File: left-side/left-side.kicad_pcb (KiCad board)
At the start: 2 copper layers, 165 x 90 mm, 4 parts, among them J1 XT60, J2 XT60, J3 RPi Power

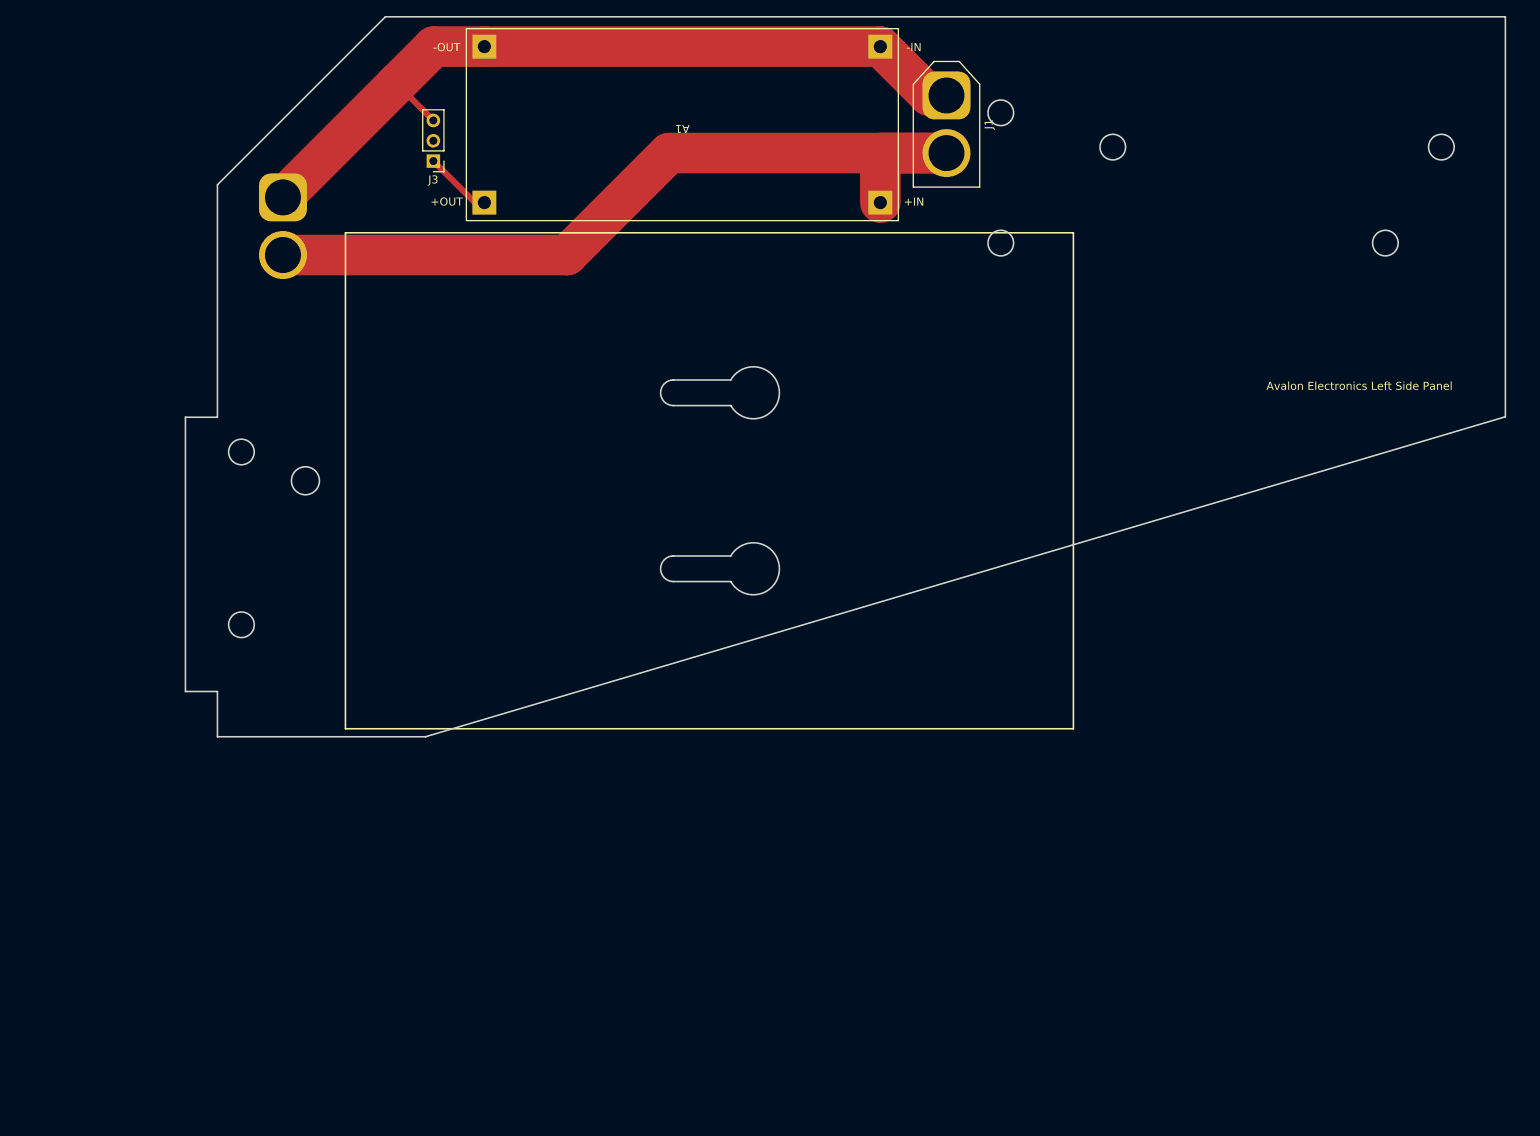
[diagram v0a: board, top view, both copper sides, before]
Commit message: update outlines, finish left side
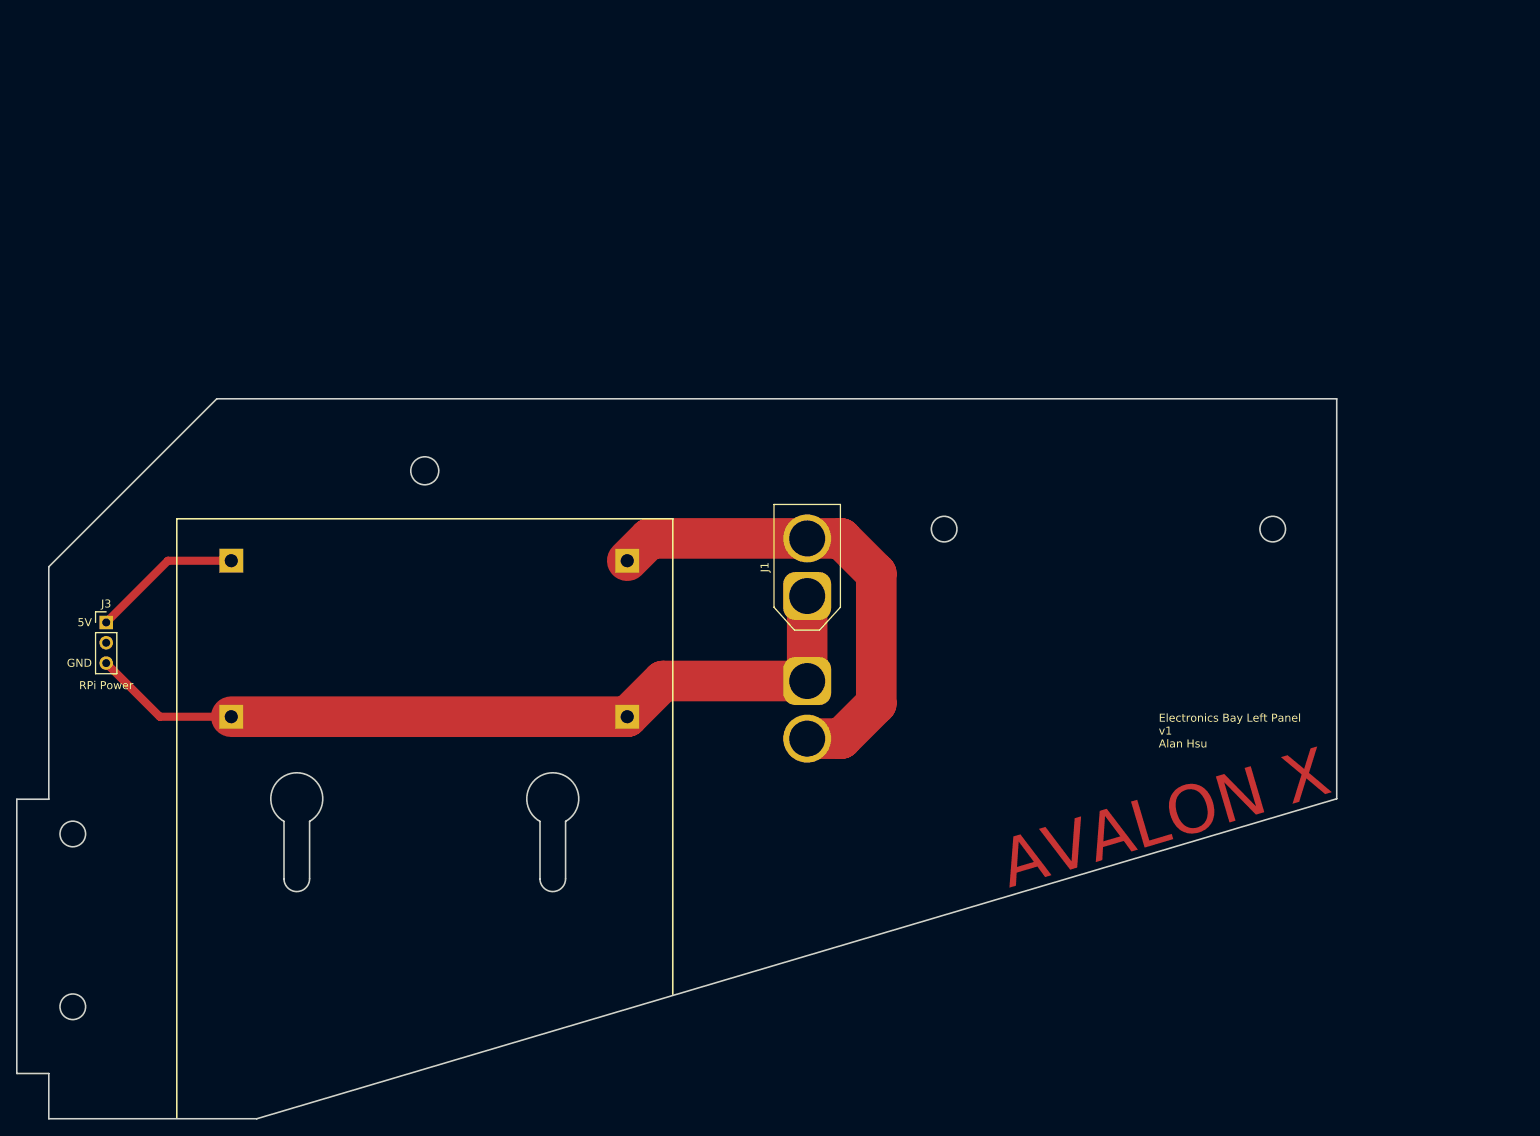
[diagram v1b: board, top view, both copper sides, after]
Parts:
- A1: moved to B.Cu
- moved J2 89.2 mm to (147.3, 123.4)
- moved A1 71.6 mm to (100.1, 118.1)
- moved J3 70.7 mm to (59.7, 116.1), turned to 0 degrees
- moved J1 65.0 mm to (147.3, 112.8), turned to 90 degrees
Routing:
- net +BATT: track 102.7 -> 60.8 mm
- net Net-(A1-VOUT): track 8.53 -> 18.8 mm
- net GND: track 99.8 -> 102.9 mm
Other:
- outline, holes or cut-outs redrawn
- board text added: "5V"
- board text added: "AVALON X"
- board text added: "Electronics Bay Left Panel v1 Alan Hsu"
- board text added: "GND"
- board text removed: "Avalon Electronics Left Side Panel"

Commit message: finalize both panels
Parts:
- moved J3 9.88 mm to (62.7, 125.5)
- moved A1 9.65 mm to (100.1, 127.8)
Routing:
- net +BATT: track 60.8 -> 64.8 mm
- net Net-(A1-VOUT): track 18.8 -> 15.7 mm
- net GND: track 102.9 -> 103.9 mm
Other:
- outline, holes or cut-outs redrawn
- board text added: "4S Battery Input"
- board text added: "Out to Right Side Panel"
- board text added: "RASPBERRY PI GOES HERE"
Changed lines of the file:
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@@
   (net 4 "unconnected-(J3-Pin_2-Pad2)")
   (footprint "Connector_PinHeader_2.54mm:PinHeader_1x03_P2.54mm_Vertical" (layer "F.Cu")
-    (at 59.69 116.078)
+    (at 62.738 125.476)
     (descr "Through hole straight pin header, 1x03, 2.54mm pitch, single row")
     (tags "Through hole pin header THT 1x03 2.54mm single row")
@@
     (property "ki_keywords" "connector")
     (attr through_hole)
-    (fp_text reference "J1" (at 3.6 -5.3 90) (layer "F.SilkS")
+    (fp_text reference "J1" (at 3.6 -5.3 90) (layer "F.SilkS") hide
         (effects (font (size 1 1) (thickness 0.15)))
     )
@@
   )
   (footprint "left-side:Buck" (layer "B.Cu")
-    (at 100.076 118.11 180)
+    (at 100.076 127.762 180)
     (property "Sheetfile" "left-side.kicad_sch")
     (property "Sheetname" "")
@@
     (property "ki_keywords" "connector")
     (attr through_hole)
-    (fp_text reference "J2" (at 3.6 5.3 90) (layer "B.SilkS")
+    (fp_text reference "J2" (at 3.6 5.3 90) (layer "B.SilkS") hide
         (effects (font (size 1 1) (thickness 0.15)) (justify mirror))
     )
@@
     )
   )
-  (gr_line (start 68.514 103.119146) (end 130.514 103.119146)
+  (gr_line (start 68.514 113.119146) (end 130.514 113.119146)
     (stroke (width 0.2) (type solid)) (layer "F.SilkS"))
-  (gr_line (start 130.514 103.119146) (end 130.514 162.56)
+  (gr_line (start 130.514 113.119146) (end 130.556 162.814)
     (stroke (width 0.2) (type solid)) (layer "F.SilkS"))
-  (gr_line (start 68.514 178.054) (end 68.514 103.119146)
+  (gr_line (start 68.514 178.054) (end 68.514 113.119146)
     (stroke (width 0.2) (type solid)) (layer "F.SilkS"))
   (gr_circle (center 150.438628 116.407873) (end 152.038628 116.407873)
@@
   (gr_line (start 48.514 138.176) (end 48.514 172.462292)
     (stroke (width 0.2) (type solid)) (layer "Edge.Cuts"))
-  (gr_line (start 52.514 172.462292) (end 52.514 178.119146)
-    (stroke (width 0.2) (type solid)) (layer "Edge.Cuts"))
-  (gr_line (start 73.514 88.119146) (end 52.514 109.119146)
+  (gr_line (start 54.514 172.462292) (end 54.514 178.119146)
+    (stroke (width 0.2) (type solid)) (layer "Edge.Cuts"))
+  (gr_line (start 75.514 88.119146) (end 54.514 109.119146)
     (stroke (width 0.2) (type solid)) (layer "Edge.Cuts"))
   (gr_circle (center 164.438628 104.407873) (end 166.038628 104.407873)
     (stroke (width 0.2) (type solid)) (fill none) (layer "Edge.Cuts"))
-  (gr_arc (start 81.914 140.948015) (mid 83.514 134.869146) (end 85.114 140.948015)
-    (stroke (width 0.2) (type solid)) (layer "Edge.Cuts"))
-  (gr_arc (start 117.114 148.119146) (mid 115.514 149.719146) (end 113.914 148.119146)
-    (stroke (width 0.2) (type solid)) (layer "Edge.Cuts"))
-  (gr_line (start 213.514 88.119146) (end 73.514 88.119146)
-    (stroke (width 0.2) (type solid)) (layer "Edge.Cuts"))
-  (gr_circle (center 99.514 97.119146) (end 101.264 97.119146)
-    (stroke (width 0.2) (type solid)) (fill none) (layer "Edge.Cuts"))
-  (gr_line (start 48.514 172.462292) (end 52.514 172.462292)
-    (stroke (width 0.2) (type solid)) (layer "Edge.Cuts"))
-  (gr_line (start 113.914 140.948015) (end 113.914 148.119146)
-    (stroke (width 0.2) (type solid)) (layer "Edge.Cuts"))
-  (gr_arc (start 113.914 140.948015) (mid 115.514 134.869146) (end 117.114 140.948015)
+  (gr_arc (start 81.914 150.948015) (mid 83.514 144.869146) (end 85.114 150.948015)
+    (stroke (width 0.2) (type solid)) (layer "Edge.Cuts"))
+  (gr_arc (start 117.114 158.119146) (mid 115.514 159.719146) (end 113.914 158.119146)
+    (stroke (width 0.2) (type solid)) (layer "Edge.Cuts"))
+  (gr_line (start 213.514 88.119146) (end 75.514 88.119146)
+    (stroke (width 0.2) (type solid)) (layer "Edge.Cuts"))
+  (gr_circle (center 99.514 107.119146) (end 101.264 107.119146)
+    (stroke (width 0.2) (type solid)) (fill none) (layer "Edge.Cuts"))
+  (gr_line (start 48.514 172.462292) (end 54.514 172.462292)
+    (stroke (width 0.2) (type solid)) (layer "Edge.Cuts"))
+  (gr_line (start 113.914 150.948015) (end 113.914 158.119146)
+    (stroke (width 0.2) (type solid)) (layer "Edge.Cuts"))
+  (gr_arc (start 113.914 150.948015) (mid 115.514 144.869146) (end 117.114 150.948015)
     (stroke (width 0.2) (type solid)) (layer "Edge.Cuts"))
   (gr_line (start 213.514 138.119146) (end 213.514 88.119146)
     (stroke (width 0.2) (type solid)) (layer "Edge.Cuts"))
-  (gr_line (start 52.514 178.119146) (end 78.514 178.119146)
-    (stroke (width 0.2) (type solid)) (layer "Edge.Cuts"))
-  (gr_line (start 85.114 148.119146) (end 85.114 140.948015)
+  (gr_line (start 54.514 178.119146) (end 78.514 178.119146)
+    (stroke (width 0.2) (type solid)) (layer "Edge.Cuts"))
+  (gr_line (start 85.114 158.119146) (end 85.114 150.948015)
     (stroke (width 0.2) (type solid)) (layer "Edge.Cuts"))
   (gr_circle (center 55.514 164.119146) (end 57.114 164.119146)
     (stroke (width 0.2) (type solid)) (fill none) (layer "Edge.Cuts"))
-  (gr_line (start 117.114 148.119146) (end 117.114 140.948015)
+  (gr_line (start 117.114 158.119146) (end 117.114 150.948015)
     (stroke (width 0.2) (type solid)) (layer "Edge.Cuts"))
   (gr_line (start 78.514 178.119146) (end 213.514 138.119146)
@@
   (gr_circle (center 55.514 142.519146) (end 57.114 142.519146)
     (stroke (width 0.2) (type solid)) (fill none) (layer "Edge.Cuts"))
-  (gr_arc (start 85.114 148.119146) (mid 83.514 149.719146) (end 81.914 148.119146)
-    (stroke (width 0.2) (type solid)) (layer "Edge.Cuts"))
-  (gr_line (start 52.514 109.119146) (end 52.514 138.176)
-    (stroke (width 0.2) (type solid)) (layer "Edge.Cuts"))
-  (gr_line (start 81.914 140.948015) (end 81.914 148.119146)
+  (gr_arc (start 85.114 158.119146) (mid 83.514 159.719146) (end 81.914 158.119146)
+    (stroke (width 0.2) (type solid)) (layer "Edge.Cuts"))
+  (gr_line (start 54.514 109.119146) (end 54.514 138.176)
+    (stroke (width 0.2) (type solid)) (layer "Edge.Cuts"))
+  (gr_line (start 81.914 150.948015) (end 81.914 158.119146)
     (stroke (width 0.2) (type solid)) (layer "Edge.Cuts"))
   (gr_circle (center 205.514 104.407873) (end 207.114 104.407873)
     (stroke (width 0.2) (type solid)) (fill none) (layer "Edge.Cuts"))
-  (gr_line (start 52.514 138.176) (end 48.514 138.176)
+  (gr_line (start 54.514 138.176) (end 48.514 138.176)
     (stroke (width 0.2) (type solid)) (layer "Edge.Cuts"))
   (gr_text "AVALON X" (at 213.36 137.922 16.5) (layer "F.Cu")
     (effects (font (size 6 6) (thickness 0.625)) (justify right bottom))
   )
-  (gr_text "GND" (at 57.912 121.158) (layer "F.SilkS")
+  (gr_text "Out to Right Side Panel" (at 141.986 127 90) (layer "B.SilkS")
+    (effects (font (size 1 1) (thickness 0.15)) (justify bottom))
+  )
+  (gr_text "GND" (at 60.96 130.556) (layer "F.SilkS")
     (effects (font (size 1 1) (thickness 0.15)) (justify right))
   )
-  (gr_text "5V" (at 57.912 116.078) (layer "F.SilkS")
+  (gr_text "5V" (at 60.96 125.476) (layer "F.SilkS")
     (effects (font (size 1 1) (thickness 0.15)) (justify right))
+  )
+  (gr_text "4S Battery Input" (at 142.24 109.982) (layer "F.SilkS")
+    (effects (font (size 1 1) (thickness 0.15)) (justify right bottom))
+  )
+  (gr_text "RASPBERRY PI GOES HERE" (at 70.358 144.526) (layer "F.SilkS")
+    (effects (font (size 3 3) (thickness 0.45)) (justify left bottom))
   )
   (gr_text "Electronics Bay Left Panel\nv1\nAlan Hsu" (at 191.262 131.826) (layer "F.SilkS")
@@
     (effects (font (size 6 6) (thickness 0.625)) (justify right bottom))
   )
+  (segment (start 147.32 105.576) (end 137.262 105.576) (width 5.08) (layer "F.Cu") (net 1))
   (segment (start 147.32 130.6) (end 151.56264 130.6) (width 5.08) (layer "F.Cu") (net 1))
+  (segment (start 137.262 105.576) (end 124.826 118.012) (width 5.08) (layer "F.Cu") (net 1))
   (segment (start 151.56264 105.576) (end 147.32 105.576) (width 5.08) (layer "F.Cu") (net 1))
-  (segment (start 147.32 105.576) (end 127.61 105.576) (width 5.08) (layer "F.Cu") (net 1))
   (segment (start 155.956 109.96936) (end 151.56264 105.576) (width 5.08) (layer "F.Cu") (net 1))
-  (segment (start 127.61 105.576) (end 124.826 108.36) (width 5.08) (layer "F.Cu") (net 1))
   (segment (start 151.56264 130.6) (end 155.956 126.20664) (width 5.08) (layer "F.Cu") (net 1))
   (segment (start 155.956 126.20664) (end 155.956 109.96936) (width 5.08) (layer "F.Cu") (net 1))
-  (segment (start 75.326 127.86) (end 124.826 127.86) (width 5.08) (layer "F.Cu") (net 2))
-  (segment (start 129.286 123.4) (end 124.826 127.86) (width 5.08) (layer "F.Cu") (net 2))
-  (segment (start 59.69 121.158) (end 66.392 127.86) (width 1.016) (layer "F.Cu") (net 2))
+  (segment (start 138.938 123.4) (end 124.826 137.512) (width 5.08) (layer "F.Cu") (net 2))
+  (segment (start 75.326 137.512) (end 124.826 137.512) (width 5.08) (layer "F.Cu") (net 2))
+  (segment (start 68.37 130.556) (end 75.326 137.512) (width 1.016) (layer "F.Cu") (net 2))
+  (segment (start 62.738 130.556) (end 68.37 130.556) (width 1.016) (layer "F.Cu") (net 2))
   (segment (start 147.32 112.776) (end 147.32 123.4) (width 5.08) (layer "F.Cu") (net 2))
-  (segment (start 66.392 127.86) (end 75.326 127.86) (width 1.016) (layer "F.Cu") (net 2))
-  (segment (start 147.32 123.4) (end 129.286 123.4) (width 5.08) (layer "F.Cu") (net 2))
-  (segment (start 75.326 108.36) (end 67.408 108.36) (width 1.016) (layer "F.Cu") (net 3))
-  (segment (start 67.408 108.36) (end 59.69 116.078) (width 1.016) (layer "F.Cu") (net 3))
+  (segment (start 147.32 123.4) (end 138.938 123.4) (width 5.08) (layer "F.Cu") (net 2))
+  (segment (start 67.862 125.476) (end 62.738 125.476) (width 1.016) (layer "F.Cu") (net 3))
+  (segment (start 75.326 118.012) (end 67.862 125.476) (width 1.016) (layer "F.Cu") (net 3))
 )
